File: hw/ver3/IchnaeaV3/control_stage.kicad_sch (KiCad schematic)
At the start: 23 parts, among them J5 FanConnector, J6 Conn_02x07_Odd_Even, Q26 BSS138, Q27 BSS84, Q28 BSS138, Q29 BSS138, Q30 BSS138

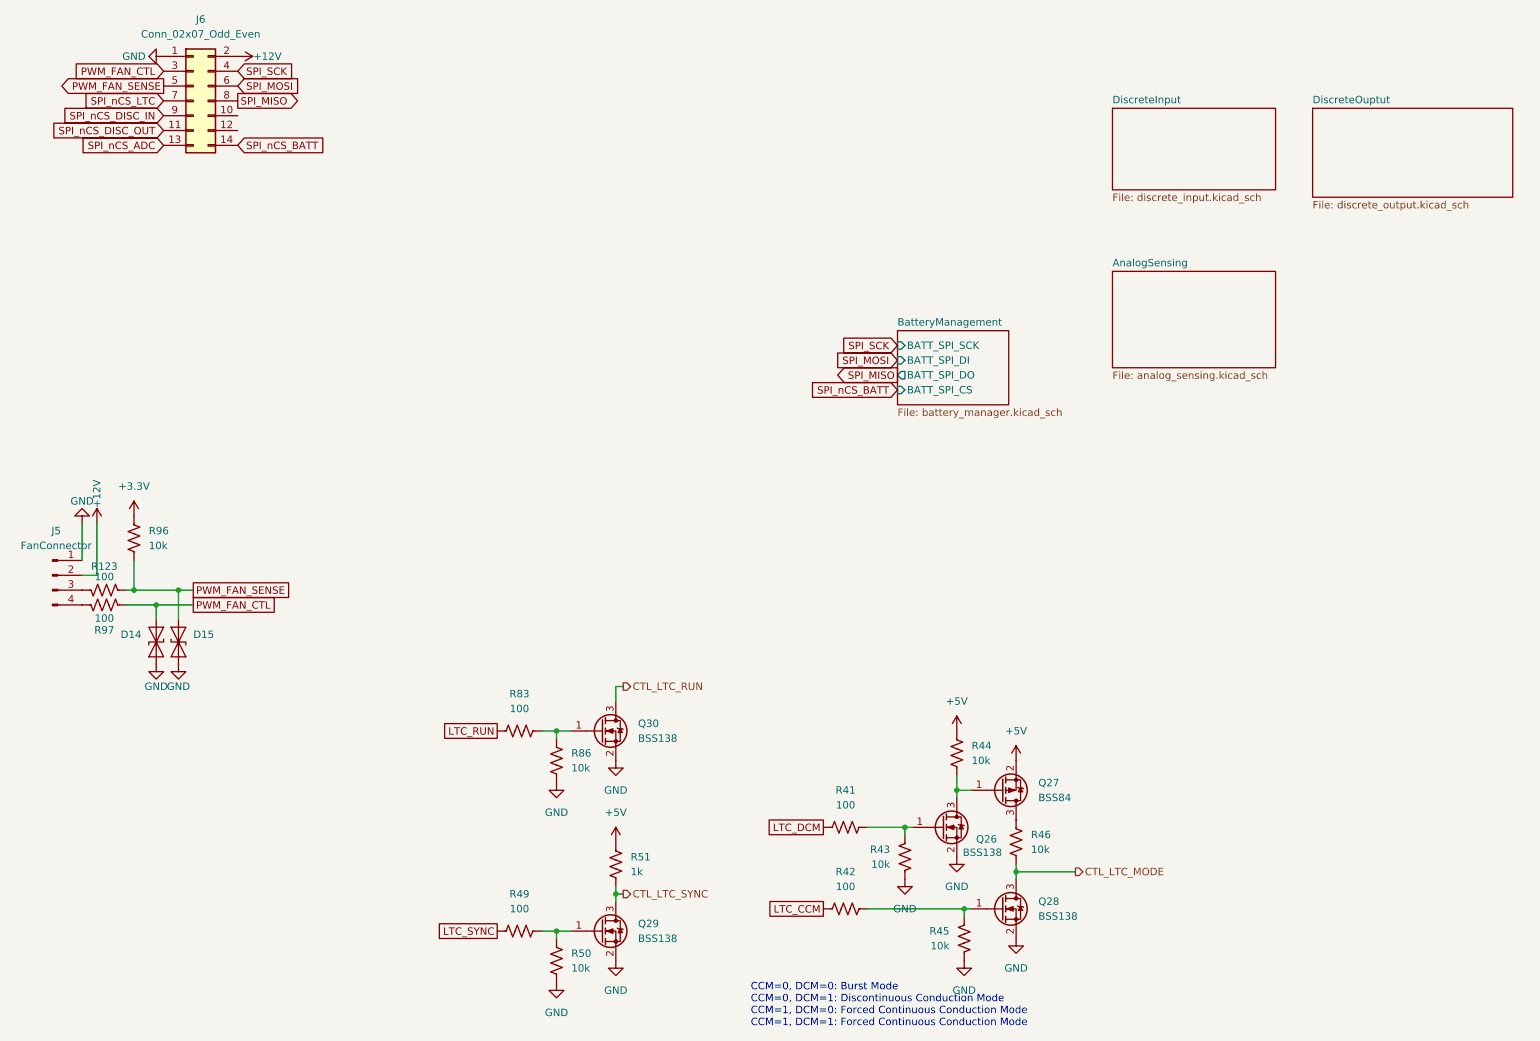
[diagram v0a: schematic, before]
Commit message: Experiment with a new power stage layout
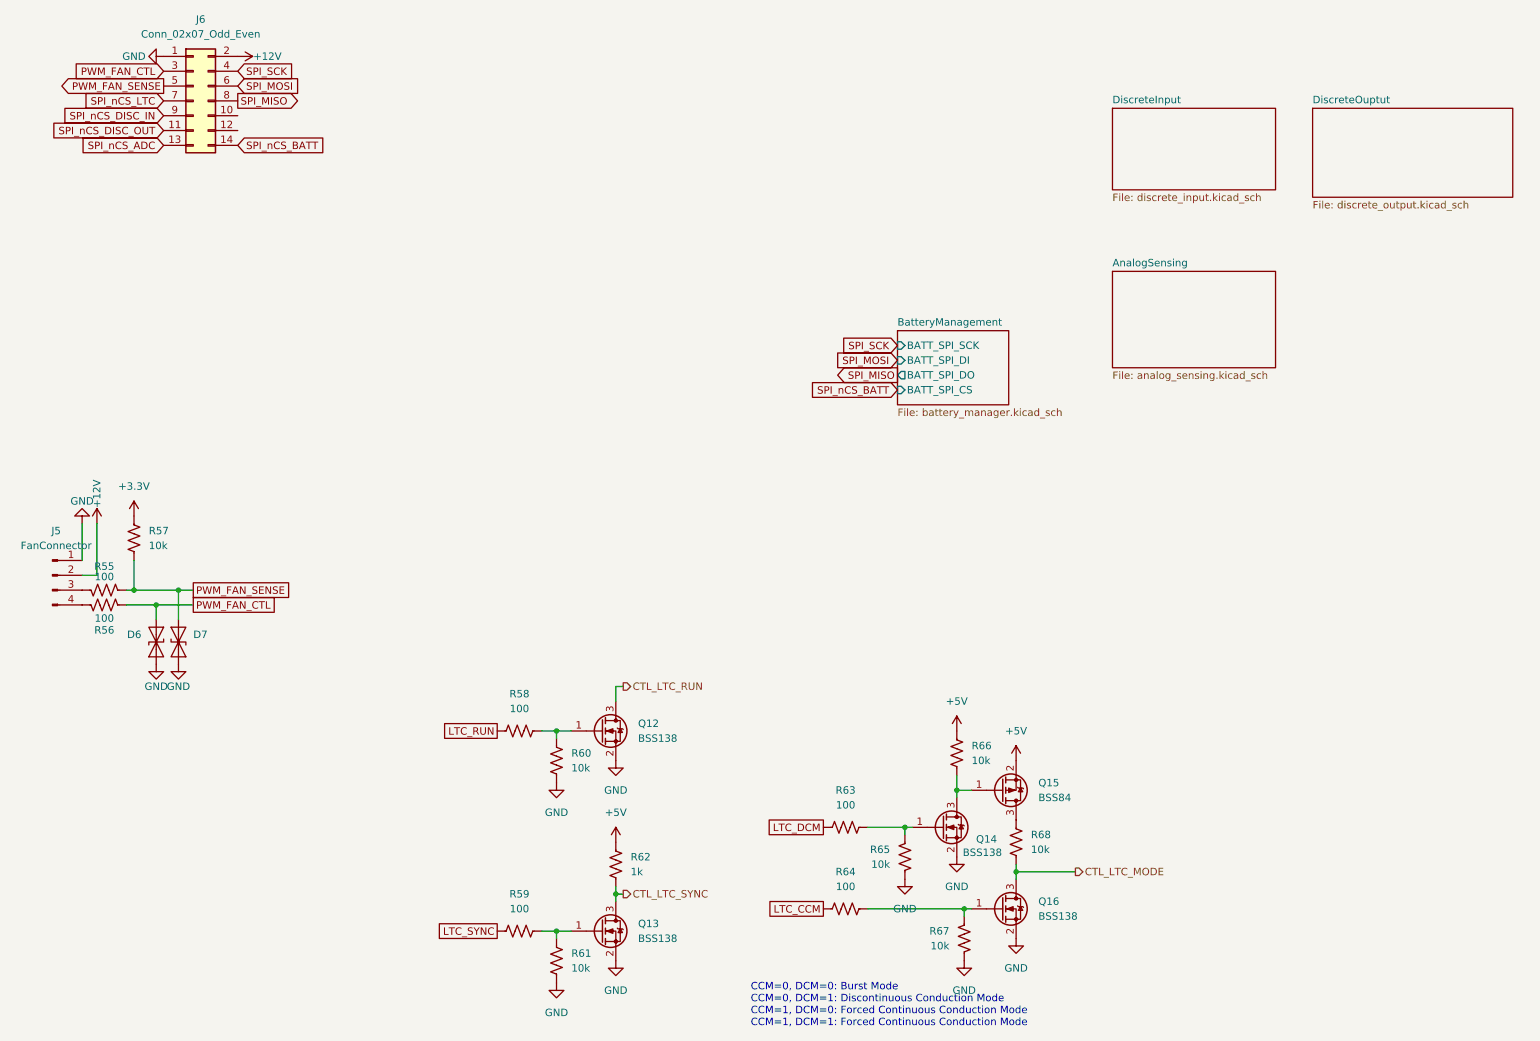
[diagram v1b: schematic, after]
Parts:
- renumbered D14 to D6, D15 to D7, Q30 to Q12, Q29 to Q13, Q26 to Q14, Q27 to Q15, Q28 to Q16, R123 to R55, R97 to R56, R96 to R57, R83 to R58, R49 to R59, R86 to R60, R50 to R61, R51 to R62, R41 to R63, R42 to R64, R43 to R65, R44 to R66, R45 to R67, R46 to R68

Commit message: Swiftly correct the design issue.
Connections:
- net +12V: no longer J6.2 (Pin_2)
- net +5V: now also J6.2 (Pin_2)
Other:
- note added: "TODO: Can I delete the 3.3v rail entirely?"
- note added: "TODO: Delete resistors on MOSFETs and let the shift register handle logic levels"
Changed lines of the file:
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@@
+		)
+	)
+	(text "TODO: Delete resistors on MOSFETs and let the \nshift register handle logic levels"
+		(exclude_from_sim no)
+		(at 156.972 143.256 0)
+		(effects
+			(font
+				(size 1.27 1.27)
+			)
 		)
 	)
@@
 		)
 	)
+	(text "TODO: Can I delete the 3.3v rail entirely?"
+		(exclude_from_sim no)
+		(at 138.684 42.164 0)
+		(effects
+			(font
+				(size 1.27 1.27)
+			)
+		)
+	)
 	(global_label "PWM_FAN_CTL"
 		(shape input)
@@
 		)
 	)
+	(hierarchical_label "ISENSE_PWR_IN"
+		(shape input)
+		(at 92.71 119.38 0)
+		(fields_autoplaced yes)
+		(effects
+			(font
+				(size 1.27 1.27)
+			)
+			(justify left)
+		)
+	)
 	(hierarchical_label "CTL_LTC_SYNC"
 		(shape output)
@@
 		(shape output)
 		(at 200.66 181.61 0)
+		(fields_autoplaced yes)
+		(effects
+			(font
+				(size 1.27 1.27)
+			)
+			(justify left)
+		)
+	)
+	(hierarchical_label "ISENSE_PWR_OUT"
+		(shape input)
+		(at 92.71 116.84 0)
 		(fields_autoplaced yes)
 		(effects
@@
 	)
 	(symbol
-		(lib_id "power:+12P")
-		(at 57.15 41.91 270)
-		(unit 1)
-		(exclude_from_sim no)
-		(in_bom yes)
-		(on_board yes)
-		(dnp no)
-		(property "Reference" "#PWR0136"
-			(at 53.34 41.91 0)
-			(effects
-				(font
-					(size 1.27 1.27)
-				)
-				(hide yes)
-			)
-		)
-		(property "Value" "+12V"
-			(at 62.23 41.91 90)
-			(effects
-				(font
-					(size 1.27 1.27)
-				)
-			)
-		)
-		(property "Footprint" ""
-			(at 57.15 41.91 0)
-			(effects
-				(font
-					(size 1.27 1.27)
-				)
-				(hide yes)
-			)
-		)
-		(property "Datasheet" ""
-			(at 57.15 41.91 0)
-			(effects
-				(font
-					(size 1.27 1.27)
-				)
-				(hide yes)
-			)
-		)
-		(property "Description" "Power symbol creates a global label with name \"+12P\""
-			(at 57.15 41.91 0)
-			(effects
-				(font
-					(size 1.27 1.27)
-				)
-				(hide yes)
-			)
-		)
-		(pin "1"
-		)
-		(instances
-			(project "IchnaeaV3"
-				(path "/93408532-1ffa-463d-873c-16289d2b7987/f8cdf9d7-add1-4ff8-8430-918a71e3d1f9"
-					(reference "#PWR0136")
-					(unit 1)
-				)
-			)
-		)
-	)
-	(symbol
 		(lib_id "Device:R_US")
 		(at 161.29 173.99 270)
@@
 					(unit 1)
 				)
+			)
+		)
+	)
+	(symbol
+		(lib_id "power:+5V")
+		(at 57.15 41.91 270)
+		(unit 1)
+		(exclude_from_sim no)
+		(in_bom yes)
+		(on_board yes)
+		(dnp no)
+		(fields_autoplaced yes)
+		(property "Reference" "#PWR0136"
+			(at 53.34 41.91 0)
+			(effects
+				(font
+					(size 1.27 1.27)
+				)
+				(hide yes)
+			)
+		)
+		(property "Value" "+5V"
+			(at 60.96 41.9099 90)
+			(effects
+				(font
+					(size 1.27 1.27)
+				)
+				(justify left)
+			)
+		)
+		(property "Footprint" ""
+			(at 57.15 41.91 0)
+			(effects
+				(font
+					(size 1.27 1.27)
+				)
+				(hide yes)
+			)
+		)
+		(property "Datasheet" ""
+			(at 57.15 41.91 0)
+			(effects
+				(font
+					(size 1.27 1.27)
+				)
+				(hide yes)
+			)
+		)
+		(property "Description" "Power symbol creates a global label with name \"+5V\""
+			(at 57.15 41.91 0)
+			(effects
+				(font
+					(size 1.27 1.27)
+				)
+				(hide yes)
+			)
+		)
+		(pin "1"
+		)
+		(instances
+			(project "IchnaeaV3"
+				(path "/93408532-1ffa-463d-873c-16289d2b7987/f8cdf9d7-add1-4ff8-8430-918a71e3d1f9"
+					(reference "#PWR0136")
+					(unit 1)
+				)

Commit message: Improve more of the power stage layout
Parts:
- removed R58, R59, R63, R64: 100, Resistor_SMD:R_0603_1608Metric, symbol Device:R_US
- removed R60, R61, R65, R67: 10k, Resistor_SMD:R_0603_1608Metric, symbol Device:R_US
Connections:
- net +3.3V is gone; now on net +5V: R57.2
- net LTC_CCM: now also Q16.1 (G)
- net LTC_DCM: now also Q14.1 (G)
- net LTC_RUN: now also Q12.1 (G)
- net LTC_SYNC: now also Q13.1 (G)
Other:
- note removed: "TODO: Can I delete the 3.3v rail entirely?"
- note removed: "TODO: Delete resistors on MOSFETs and let the shift register handle logic levels"
